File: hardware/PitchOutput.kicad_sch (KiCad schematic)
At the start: 28 parts, among them J3 Pitch, J8 CC, U3 TL072, U4 TL072

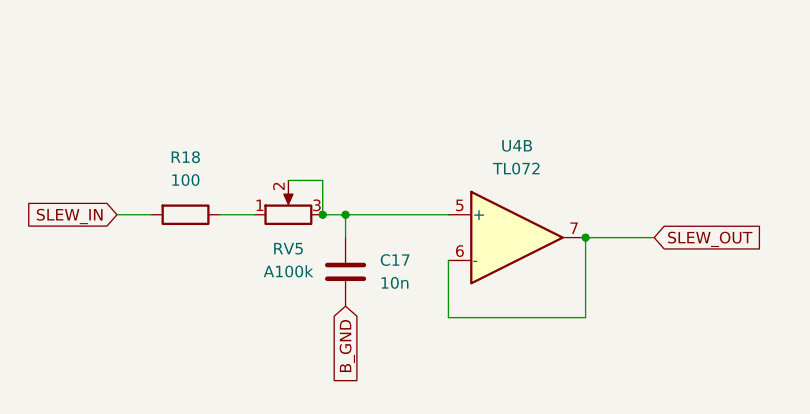
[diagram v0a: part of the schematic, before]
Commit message: main board rev 4: fix midi thru, led arrangement, glide cap value. fix sync trigger output
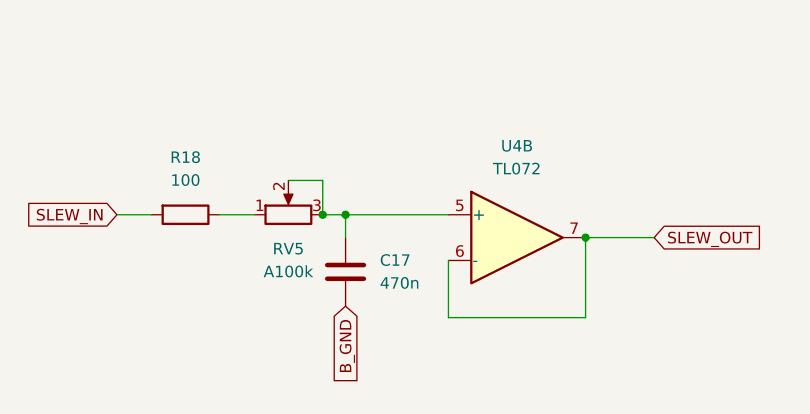
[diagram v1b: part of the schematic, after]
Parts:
- C17: value 10n -> 470n; LCSC C57112 -> C1623
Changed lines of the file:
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@@
 	(paper "A4")
 	(title_block
-		(rev "3")
+		(rev "4")
 	)
 	(text "Slew"
@@
 			)
 		)
-		(property "Value" "10n"
+		(property "Value" "470n"
 			(at 125.73 130.8099 0)
 			(effects
@@
 			)
 		)
-		(property "LCSC" "C57112"
+		(property "LCSC" "C1623"
 			(at 121.92 129.54 0)
 			(effects
